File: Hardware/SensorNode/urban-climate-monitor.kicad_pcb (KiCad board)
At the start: 2 copper layers, 54.6 x 74.3 mm, 48 parts, among them J1 Conn_ARM_JTAG_SWD_10, U1 AAT1217, U2 TPS27081A, U3 SHT31-DIS, U4 24LC32, U5 TSD305, U6 ADG633YCP, U7 TSV911RILT, U8 RFM95W, U9 STM32L412KB

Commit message: Add photo enable pin, add deployment compose
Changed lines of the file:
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@@
     (tags "capacitor handsolder")
     (attr smd)
-    (fp_text reference C9 (at 2.9845 0.0635) (layer F.SilkS)
+    (fp_text reference C9 (at -0.8255 1.905) (layer F.SilkS)
       (effects (font (size 1 1) (thickness 0.15)))
     )

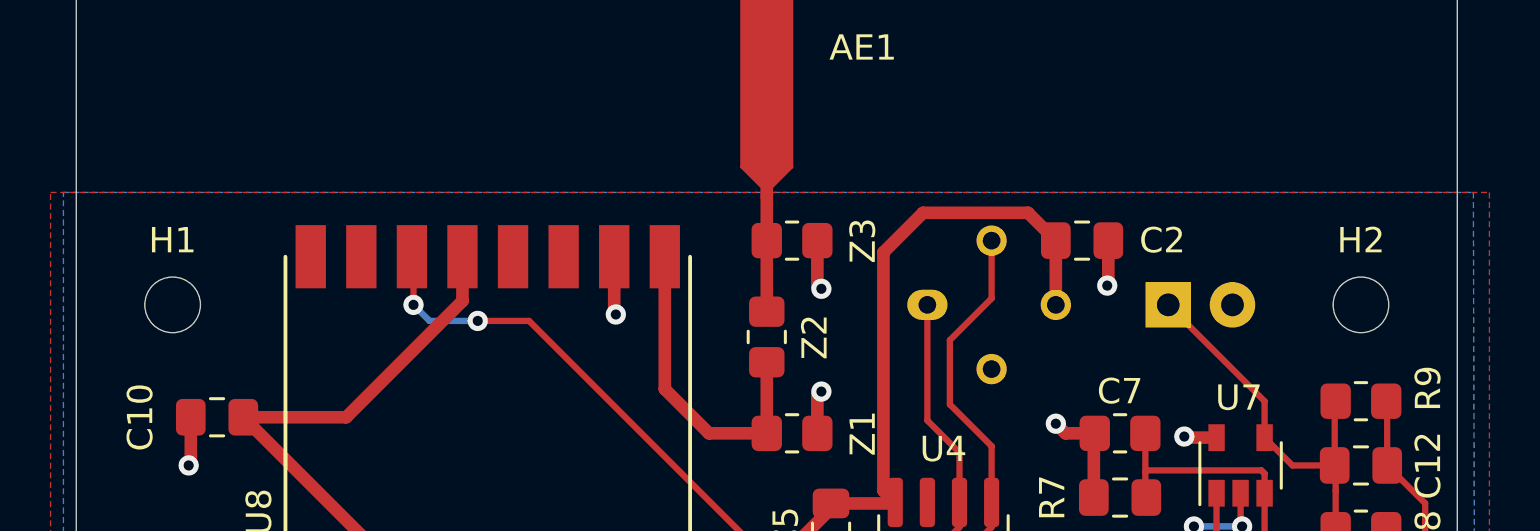
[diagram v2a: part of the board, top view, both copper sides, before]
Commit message: Upload only pdfs as artifact
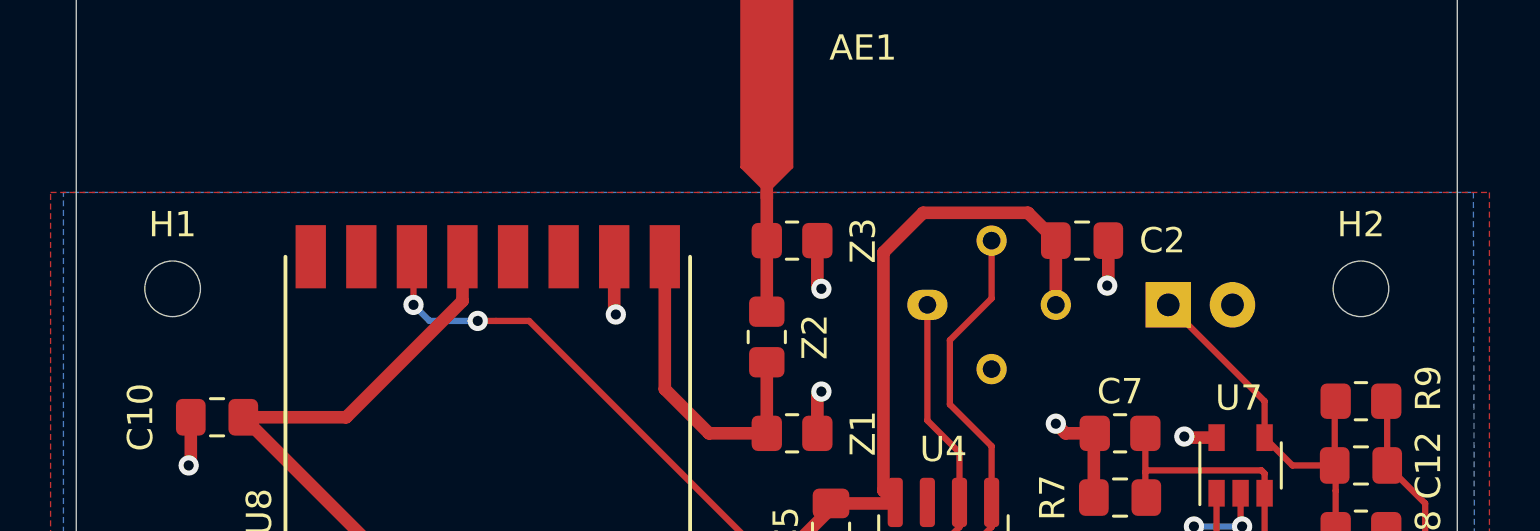
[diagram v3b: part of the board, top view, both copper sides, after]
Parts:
- moved H1 0.63 mm to (100.3, 66.0)
- moved H2 0.63 mm to (147.3, 66.0)
